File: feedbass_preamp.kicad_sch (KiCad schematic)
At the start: 16 parts, among them J2 Conn_Coaxial, U7 OPA1642

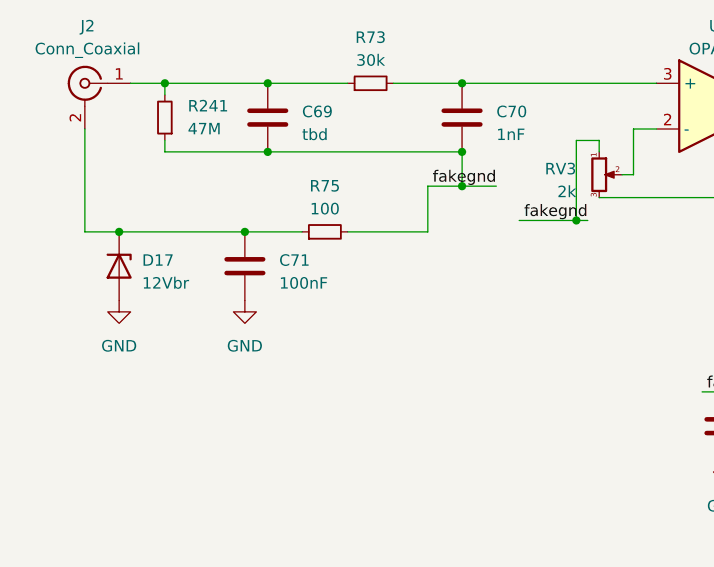
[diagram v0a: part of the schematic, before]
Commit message: updates for better bom
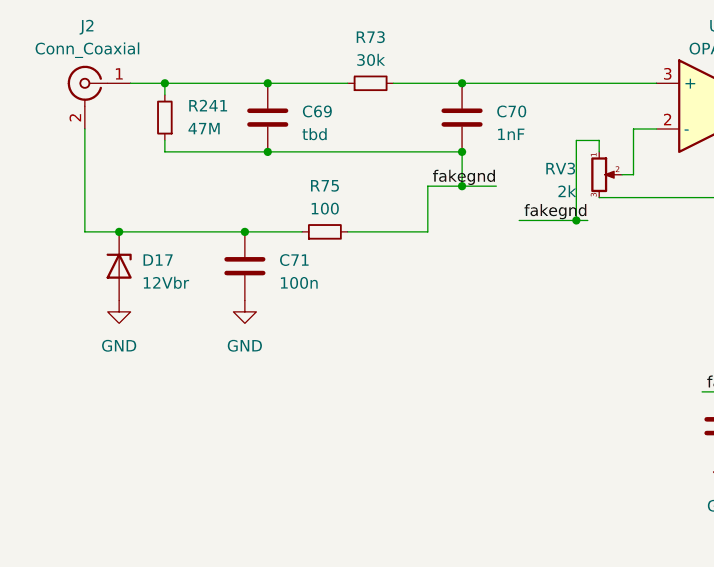
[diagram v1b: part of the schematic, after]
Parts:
- C71: value 100nF -> 100n
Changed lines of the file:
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@@
 			)
 		)
-		(property "Value" "100nF"
+		(property "Value" "100n"
 			(at 83.82 69.215 0)
 			(effects
